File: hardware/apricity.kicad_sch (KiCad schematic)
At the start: 27 parts, among them J1 USB_C_Receptacle_USB2.0, U1 ESP-WROOM-02D, U2 X

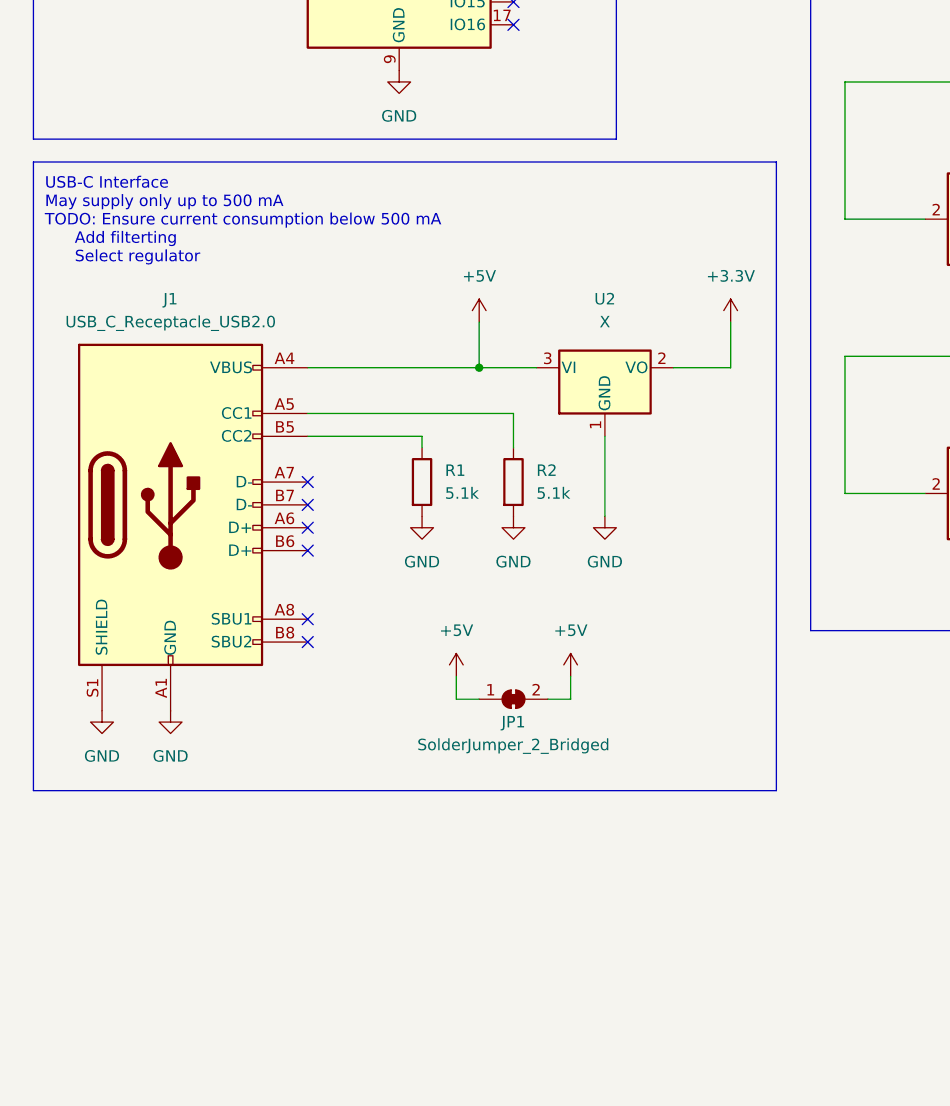
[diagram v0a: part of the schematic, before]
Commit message: flesh out power regulation
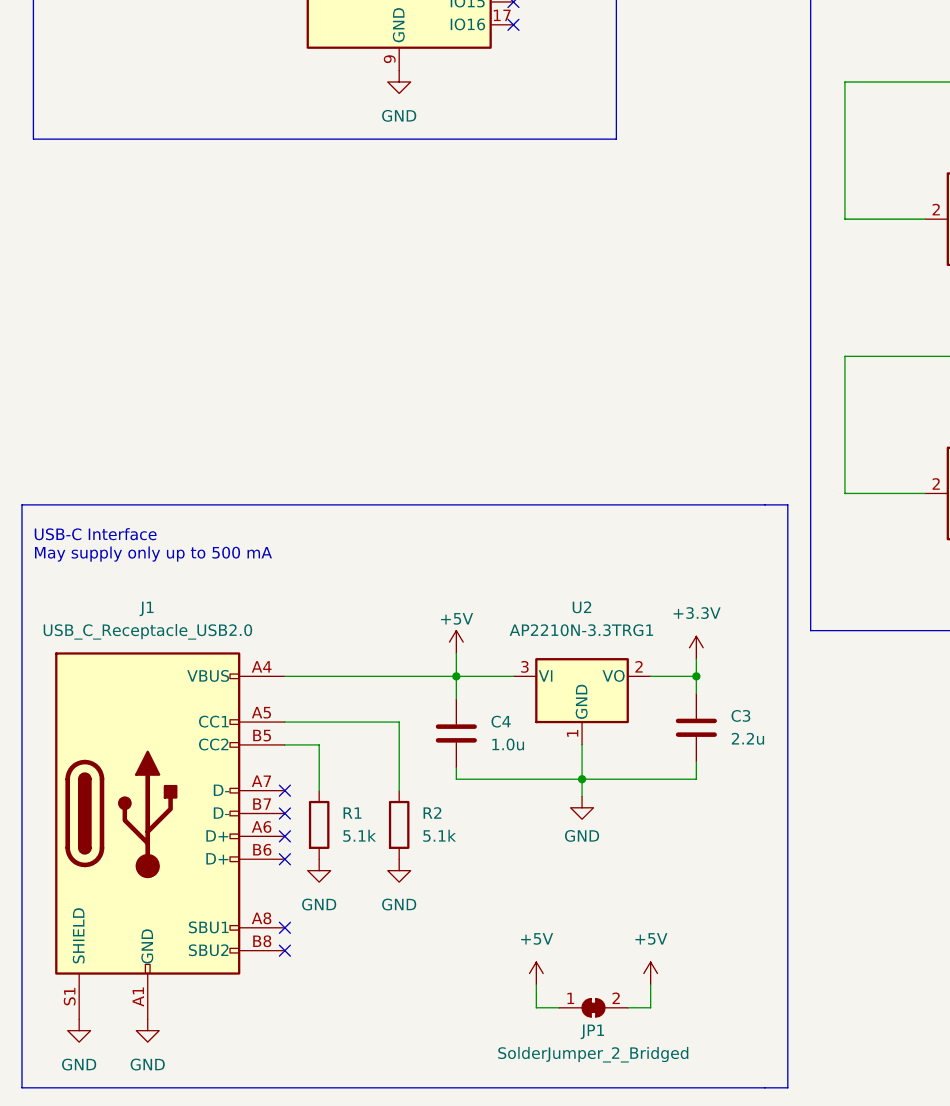
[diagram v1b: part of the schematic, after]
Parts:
- removed U2: X, Package_TO_SOT_SMD:TSOT-23_HandSoldering, symbol Regulator_Linear:AMS1117-3.3
- added C3: 2.2u, symbol Device:C
- added C4: 1.0u, symbol Device:C
- added U2: AP2210N-3.3TRG1, Package_TO_SOT_SMD:TSOT-23_HandSoldering, symbol Regulator_Linear:MCP1703A-3302_SOT23
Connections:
- net +3.3V: now also C3.1, U2.2 (VO)
- net +5V: now also C4.1, U2.3 (VI)
- net GND: now also C3.2, C4.2, U2.1 (GND)
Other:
- note added: "USB-C Interface May supply only up to 500 mA"
- note removed: "USB-C Interface May supply only up to 500 mA TODO: Ensure current consumption below 500 mA Add filterting Select regulator"
- moved on the sheet: J1, JP1, R1, R2

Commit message: refine power as per esp datasheet
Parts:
- added C3: 0.1u, Capacitor_SMD:C_1206_3216Metric_Pad1.33x1.80mm_HandSolder, symbol Device:C
- added R1: 10k, Resistor_SMD:R_0805_2012Metric_Pad1.20x1.40mm_HandSolder, symbol Device:R
- C1, C2: footprint Capacitor_SMD:C_1206_3216Metric -> Capacitor_SMD:C_1206_3216Metric_Pad1.33x1.80mm_HandSolder
- C4: renamed from C3; footprint (none) -> Capacitor_SMD:C_1206_3216Metric_Pad1.33x1.80mm_HandSolder
- C5: renamed from C4; footprint (none) -> Capacitor_SMD:C_1206_3216Metric_Pad1.33x1.80mm_HandSolder
- renumbered R1 to R2, R2 to R3
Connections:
- net +3.3V: now also R1.1; no longer U1.2 (EN)
- net GND: now also U1.15 (RST), C3.2
- new net: C3.1, R1.2, U1.2 (EN)
- no-connect marks 19 -> 18

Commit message: add peripherals for programming
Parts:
- added J1: Conn_01x02_Male, Connector_PinHeader_2.54mm:PinHeader_1x02_P2.54mm_Vertical, symbol Connector:Conn_01x02_Male
- added J2: Conn_01x03_Male, Connector_PinHeader_2.54mm:PinHeader_1x03_P2.54mm_Vertical, symbol Connector:Conn_01x03_Male
- added R3: 10k, Resistor_SMD:R_0805_2012Metric_Pad1.20x1.40mm_HandSolder, symbol Device:R
- renumbered J1 to J3, R1 to R2, R2 to R4, R3 to R5
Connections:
- net GND: now also J2.1 (Pin_1), R3.2
- net at U1.11 (RXD): now also J2.3 (Pin_3)
- net at U1.12 (TXD): now also J2.2 (Pin_2)
- net at U1.8 (IO0): now also J1.2 (Pin_2)
- new net: J1.1 (Pin_1), R3.1
- no-connect marks 18 -> 15
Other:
- note added: "Boot mode"
- note added: "UART Download"

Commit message: add boot mode in schematic
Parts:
- renumbered R2 to R1, R3 to R2, R4 to R3, R5 to R4

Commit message: add buttons for program and reset
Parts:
- removed J1: Conn_01x02_Male, Connector_PinHeader_2.54mm:PinHeader_1x02_P2.54mm_Vertical, symbol Connector:Conn_01x02_Male
- added R1: 100, Resistor_SMD:R_0805_2012Metric_Pad1.20x1.40mm_HandSolder, symbol Device:R
- added R3: 10k, Resistor_SMD:R_0805_2012Metric_Pad1.20x1.40mm_HandSolder, symbol Device:R
- added SW1: Reset, Button_Switch_SMD:SW_SPST_CK_RS282G05A3, symbol Switch:SW_Push
- added SW2: Prog, Button_Switch_SMD:SW_SPST_CK_RS282G05A3, symbol Switch:SW_Push
- U2: footprint Package_TO_SOT_SMD:TSOT-23_HandSoldering -> Package_TO_SOT_SMD:SOT-23_Handsoldering
- renumbered J2 to J1, J3 to J2, R1 to R2, R2 to R4, R3 to R5, R4 to R6
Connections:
- net +3.3V: now also R1.1
- net GND: now also R3.2; no longer U1.15 (RST)
- net at U1.8 (IO0): now also SW2.1
- net at R4.1: now also SW2.2
- new net: R3.1, SW1.1, U1.15 (RST)
- new net: R1.2, SW1.2
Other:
- note removed: "Boot mode"
- note removed: "UART Download"
- moved on the sheet: C1, C2, C3, J1, R2, R4, U1

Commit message: switch to horizontal programmer
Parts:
- J1: footprint Connector_PinHeader_2.54mm:PinHeader_1x03_P2.54mm_Vertical -> Connector_PinHeader_2.54mm:PinHeader_1x03_P2.54mm_Horizontal
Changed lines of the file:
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@@
       (effects (font (size 1.27 1.27)) (justify right) hide)
     )
-    (property "Footprint" "Connector_PinHeader_2.54mm:PinHeader_1x03_P2.54mm_Vertical" (id 2) (at 32.385 84.455 0)
+    (property "Footprint" "Connector_PinHeader_2.54mm:PinHeader_1x03_P2.54mm_Horizontal" (id 2) (at 32.385 84.455 0)
       (effects (font (size 1.27 1.27)) hide)
     )
@@
     )
     (path "/eac6142d-6ea4-49f4-a1dd-0829f5302979"
-      (reference "J1") (unit 1) (value "Conn_01x03_Male") (footprint "Connector_PinHeader_2.54mm:PinHeader_1x03_P2.54mm_Vertical")
+      (reference "J1") (unit 1) (value "Conn_01x03_Male") (footprint "Connector_PinHeader_2.54mm:PinHeader_1x03_P2.54mm_Horizontal")
     )
     (path "/efec80d5-3b93-449b-967c-e6308c2f145f"

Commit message: add capacitors for LEDs
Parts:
- added C1, C10, C13, C14, C15, C16, C17, C18, C19, C2, C20, C21, C3, C4, C5, C8, C9: 0.1u, Capacitor_SMD:C_1206_3216Metric_Pad1.33x1.80mm_HandSolder, symbol Device:C
- renumbered C3 to C12, C4 to C22, C5 to C23, C1 to C6, C2 to C7
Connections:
- net +5V: now also C1.1, C10.1, C13.1, C14.1, C15.1, C16.1, C17.1, C18.1, C19.1, C2.1, C20.1, C21.1, C3.1, C4.1, C5.1, C8.1, C9.1
- net GND: now also C1.2, C10.2, C13.2, C14.2, C15.2, C16.2, C17.2, C18.2, C19.2, C2.2, C20.2, C21.2, C3.2, C4.2, C5.2, C8.2, C9.2

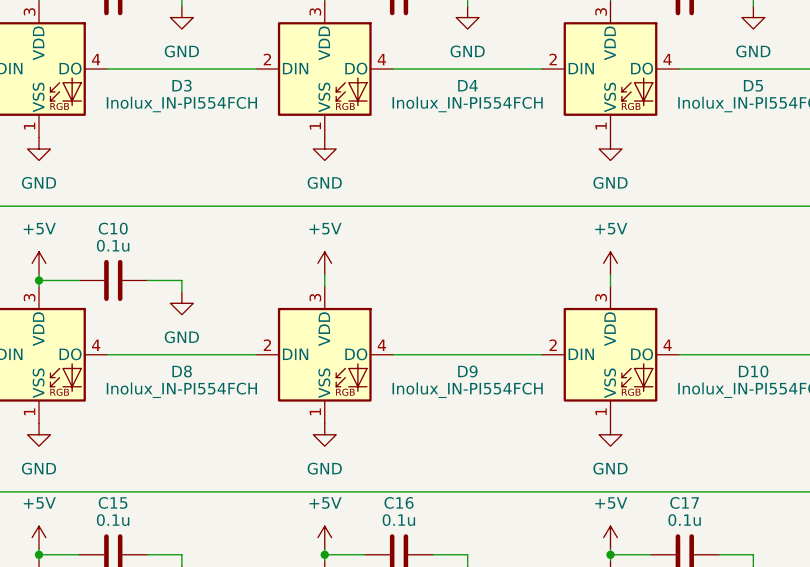
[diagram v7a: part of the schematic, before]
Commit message: add back in capacitor for D1
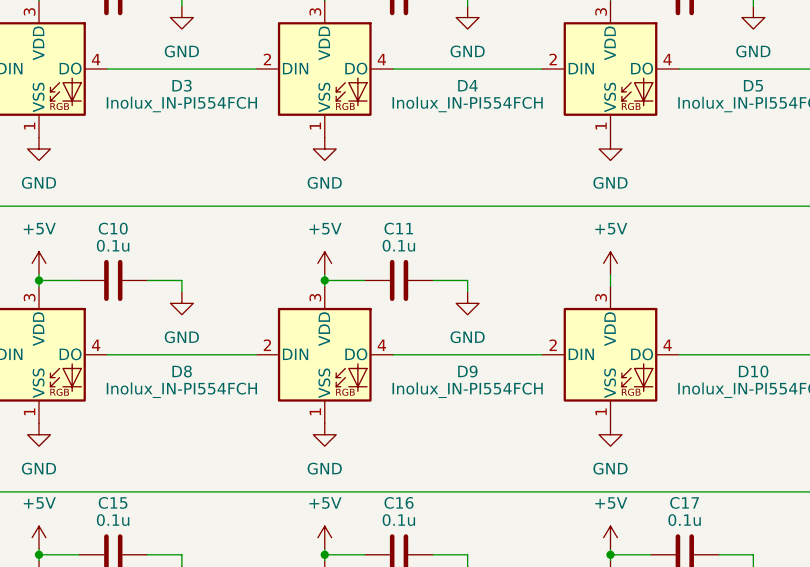
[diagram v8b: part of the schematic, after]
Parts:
- added C11: 0.1u, Capacitor_SMD:C_1206_3216Metric_Pad1.33x1.80mm_HandSolder, symbol Device:C
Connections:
- net +5V: now also C11.1
- net GND: now also C11.2
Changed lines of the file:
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@@
   (junction (at 217.17 28.575) (diameter 0) (color 0 0 0 0)
+  )
+  (junction (at 217.17 60.325) (diameter 0) (color 0 0 0 0)
   )
   (junction (at 121.92 60.325) (diameter 0) (color 0 0 0 0)
@@
     (stroke (width 0) (type default) (color 0 0 0 0))
   )
+  (wire (pts (xy 229.235 60.325) (xy 233.045 60.325))
+    (stroke (width 0) (type default) (color 0 0 0 0))
+  )
   (wire (pts (xy 185.42 120.65) (xy 185.42 121.285))
     (stroke (width 0) (type default) (color 0 0 0 0))
@@
     (stroke (width 0) (type default) (color 0 0 0 0))
   )
+  (wire (pts (xy 217.17 60.325) (xy 217.17 60.96))
+    (stroke (width 0) (type default) (color 0 0 0 0))
+  )
   (wire (pts (xy 217.17 28.575) (xy 221.615 28.575))
     (stroke (width 0) (type default) (color 0 0 0 0))
   )
+  (wire (pts (xy 217.17 60.325) (xy 221.615 60.325))
+    (stroke (width 0) (type default) (color 0 0 0 0))
+  )
   (wire (pts (xy 185.42 90.805) (xy 185.42 91.44))
     (stroke (width 0) (type default) (color 0 0 0 0))
@@
     (stroke (width 0) (type default) (color 0 0 0 0))
   )
+  (wire (pts (xy 233.045 61.595) (xy 233.045 60.325))
+    (stroke (width 0) (type default) (color 0 0 0 0))
+  )
   (wire (pts (xy 19.685 33.02) (xy 19.685 36.83))
     (stroke (width 0) (type default) (color 0 0 0 0))
@@
     (stroke (width 0) (type default) (color 0 0 0 0))
   )
-  (wire (pts (xy 217.17 59.69) (xy 217.17 60.96))
+  (wire (pts (xy 217.17 59.69) (xy 217.17 60.325))
     (stroke (width 0) (type default) (color 0 0 0 0))
   )
@@
     (pin "1")
   )
+  (symbol (lib_id "power:GND") (at 233.045 61.595 0) (unit 1)
+    (in_bom yes) (on_board yes) (fields_autoplaced)
+    (property "Reference" "#PWR029" (id 0) (at 233.045 67.945 0)
+      (effects (font (size 1.27 1.27)) hide)
+    )
+    (property "Value" "GND" (id 1) (at 233.045 66.675 0))
+    (property "Footprint" "" (id 2) (at 233.045 61.595 0)
+      (effects (font (size 1.27 1.27)) hide)
+    )
+    (property "Datasheet" "" (id 3) (at 233.045 61.595 0)
+      (effects (font (size 1.27 1.27)) hide)
+    )
+    (pin "1")
+  )
   (symbol (lib_id "Device:C") (at 193.675 28.575 90) (unit 1)
     (in_bom yes) (on_board yes)
@@
     )
     (property "Datasheet" "~" (id 3) (at 161.925 60.325 0)
+      (effects (font (size 1.27 1.27)) hide)
+    )
+    (pin "1")
+    (pin "2")
+  )
+  (symbol (lib_id "Device:C") (at 225.425 60.325 90) (unit 1)
+    (in_bom yes) (on_board yes)
+    (property "Reference" "C11" (id 0) (at 225.425 54.61 90))
+    (property "Value" "0.1u" (id 1) (at 225.425 56.515 90))
+    (property "Footprint" "Capacitor_SMD:C_1206_3216Metric_Pad1.33x1.80mm_HandSolder" (id 2) (at 229.235 59.3598 0)
+      (effects (font (size 1.27 1.27)) hide)
+    )
+    (property "Datasheet" "~" (id 3) (at 225.425 60.325 0)
       (effects (font (size 1.27 1.27)) hide)
     )
@@
       (reference "#PWR028") (unit 1) (value "GND") (footprint "")
     )
+    (path "/1789c5cb-21d7-4379-bcd9-ba3913cdbfe0"
+      (reference "#PWR029") (unit 1) (value "GND") (footprint "")
+    )
     (path "/b873e225-e9dc-4f29-9b8f-348ecd4e5ac3"
       (reference "#PWR030") (unit 1) (value "GND") (footprint "")
@@
       (reference "C10") (unit 1) (value "0.1u") (footprint "Capacitor_SMD:C_1206_3216Metric_Pad1.33x1.80mm_HandSolder")
     )
+    (path "/bc00a868-2689-4518-a973-3369786e8291"
+      (reference "C11") (unit 1) (value "0.1u") (footprint "Capacitor_SMD:C_1206_3216Metric_Pad1.33x1.80mm_HandSolder")
+    )
     (path "/a1f0fc0c-c4d6-4b77-92a6-285726f38c1c"
